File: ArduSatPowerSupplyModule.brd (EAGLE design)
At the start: 95.5 x 90.3 mm, 168 parts, among them IC1 ATmega328P, IC10 TMP102, IC11 TMP102, IC2 ATMEGA16U2-MU, IC3 LTC3115, IC4 LTC4078, IC5 MAX17043G+U, IC6 MAX4372F, IC7 LTC3536, IC8 MAX4372F, IC9 LTC3536, Q1 RJU003N03 N-MOSFET, Q2 RJU003N03 N-MOSFET, Q3 MOSFET-PCHANNELSMT2, Q4 RJU003N03 N-MOSFET, Q5 RJU003N03 N-MOSFET, Q6 RJU003N03 N-MOSFET, Q7 RJU003N03 N-MOSFET, Q8 RJU003N03 N-MOSFET, Q9 RJU003N03 N-MOSFET, SW1 RESET, SW2 SWITCH-SPDT

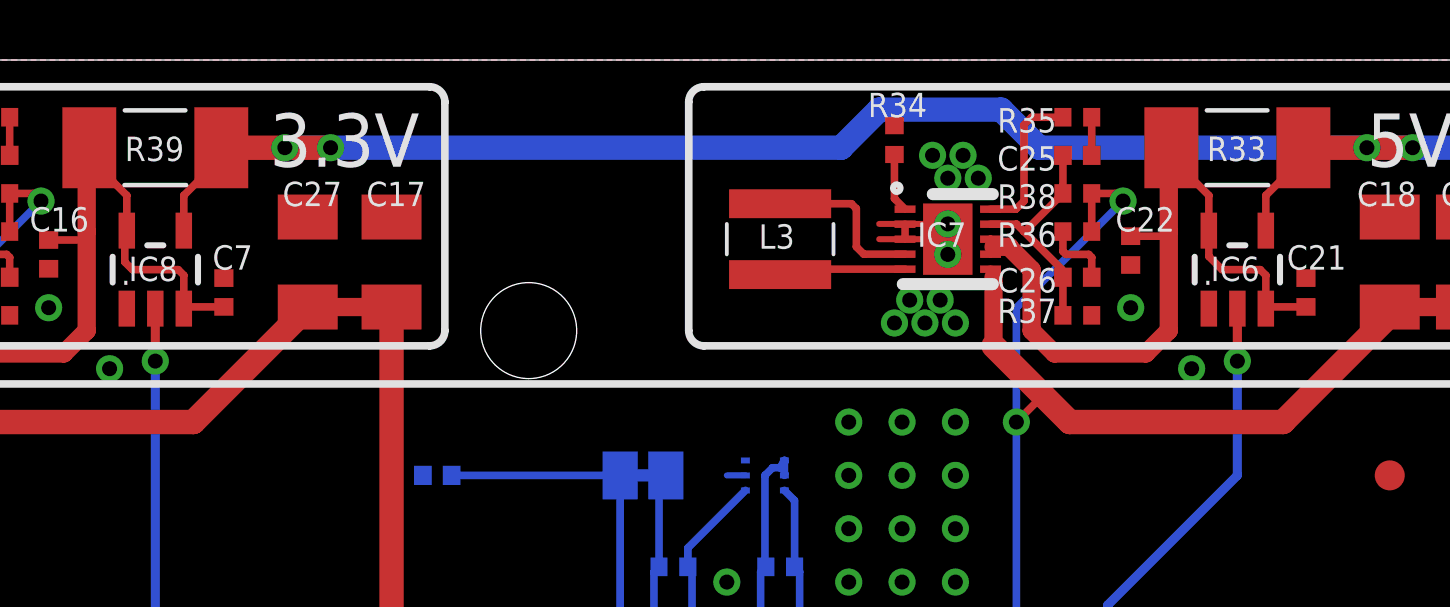
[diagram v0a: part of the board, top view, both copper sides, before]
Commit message: Changed current sense chip VCC to 5V
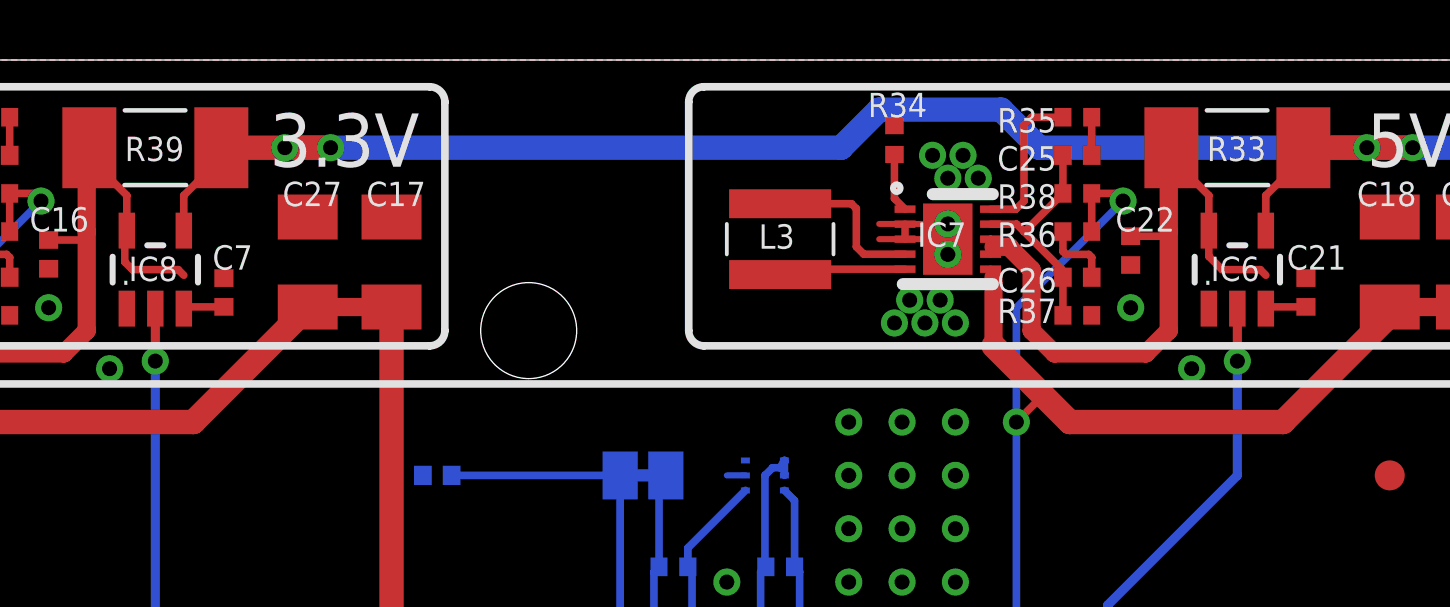
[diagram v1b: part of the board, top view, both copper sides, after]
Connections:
- net 3V3SENSED: no longer C7.1, IC8.3
- net 5V: now also C21.1, C7.1, IC6.3, IC8.3
- net 5VSENSED: no longer C21.1, IC6.3
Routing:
- net 5V: track 232.3 -> 235.0 mm
- net 5VSENSED: track 25.6 -> 23.1 mm
- net 3V3SENSED: track 26.2 -> 23.8 mm
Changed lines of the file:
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@@
 <wire x1="64.008" y1="85.852" x2="63.218" y2="85.852" width="0.254" layer="1"/>
 <contactref element="SJ4" pad="1"/>
-<wire x1="69.596" y1="45.72" x2="69.596" y2="43.18" width="0" layer="19" extent="1-1"/>
+<contactref element="C21" pad="1"/>
+<contactref element="IC6" pad="3"/>
+<wire x1="70.358" y1="82.07" x2="69.0801" y2="82.07" width="0.254" layer="1"/>
+<wire x1="69.0801" y1="82.07" x2="69.022" y2="82.0119" width="0.254" layer="1"/>
+<contactref element="IC8" pad="3"/>
+<contactref element="C7" pad="1"/>
+<wire x1="34.29" y1="82.07" x2="33.0121" y2="82.07" width="0.254" layer="1"/>
+<wire x1="33.0121" y1="82.07" x2="32.954" y2="82.0119" width="0.254" layer="1"/>
+<wire x1="73.152" y1="82.066" x2="70.358" y2="82.07" width="0" layer="19" extent="1-1"/>
+<wire x1="69.596" y1="43.18" x2="69.596" y2="45.72" width="0" layer="19" extent="1-1"/>
+<wire x1="34.29" y1="82.07" x2="48.514" y2="67.056" width="0" layer="19" extent="1-16"/>
 </signal>
 <signal name="N$1">
@@
 </signal>
 <signal name="3V3SENSED">
-<contactref element="IC8" pad="3"/>
-<contactref element="C7" pad="1"/>
 <contactref element="IC8" pad="5"/>
 <contactref element="R39" pad="2"/>
@@
 <contactref element="IC9" pad="8"/>
 <wire x1="23.777" y1="84.328" x2="23.777" y2="83.828" width="0.254" layer="1"/>
-<wire x1="34.29" y1="82.07" x2="33.0121" y2="82.07" width="0.254" layer="1"/>
-<wire x1="33.0121" y1="82.07" x2="32.954" y2="82.0119" width="0.254" layer="1"/>
-<wire x1="32.954" y1="82.0119" x2="32.954" y2="83.124" width="0.254" layer="1"/>
 <wire x1="32.954" y1="83.124" x2="32.766" y2="83.312" width="0.254" layer="1"/>
 <wire x1="32.766" y1="83.312" x2="31.242" y2="83.312" width="0.254" layer="1"/>
@@
 <contactref element="IC7" pad="8"/>
 <contactref element="R33" pad="2"/>
-<contactref element="C21" pad="1"/>
-<contactref element="IC6" pad="3"/>
 <contactref element="IC6" pad="5"/>
 <wire x1="59.845" y1="84.328" x2="59.845" y2="83.828" width="0.254" layer="1"/>
-<wire x1="69.022" y1="82.0119" x2="69.022" y2="83.124" width="0.254" layer="1"/>
 <wire x1="69.022" y1="83.124" x2="68.834" y2="83.312" width="0.254" layer="1"/>
 <wire x1="68.834" y1="83.312" x2="67.564" y2="83.312" width="0.254" layer="1"/>
@@
 <wire x1="66.548" y1="86.36" x2="66.294" y2="86.36" width="0.254" layer="1"/>
 <wire x1="66.294" y1="86.36" x2="65.786" y2="86.868" width="0.254" layer="1"/>
-<wire x1="70.358" y1="82.07" x2="69.0801" y2="82.07" width="0.254" layer="1"/>
-<wire x1="69.0801" y1="82.07" x2="69.022" y2="82.0119" width="0.254" layer="1"/>
 <wire x1="64.516" y1="84.427" x2="65.758" y2="84.427" width="0.254" layer="1"/>
 <wire x1="65.758" y1="84.427" x2="65.786" y2="84.582" width="0.254" layer="1"/>

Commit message: Relabelled board from ArduSat to LibreSat
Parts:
- removed Q3: MOSFET-PCHANNELSMT2, freetronics-jon:DPAK
- removed R27: 1K, freetronics-jon:0402
- removed R28: 33K, freetronics-jon:0402
- R11, R25: value 2K2 0402 -> 3K3 0402
- R12, R26: value 1K 0402 -> 1K5 0402
- moved JP10 10.2 mm to (19.8, 23.4), turned to 90 degrees
- moved JP11 5.08 mm to (19.8, 31.0), turned to 90 degrees
- moved C36 1.27 mm to (40.1, 76.5)
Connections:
- removed net N$4: JP11.2, R27.1
- removed net N$7: Q3.1, R27.2, R28.2
- net A2: no longer SJ19.2
- net A3: no longer SJ18.2
- net A6: now also SJ19.2
- net A7: now also SJ18.2
- net GND: no longer JP10.1
- net N$5: now also JP10.1; no longer Q3.3, R28.1
- net VBATT: now also JP11.2; no longer Q3.2
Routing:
- net A7: track 19.8 -> 47.8 mm
- net A6: track 27.5 -> 52.8 mm
- net A3: track 25.2 -> 6.10 mm
- net A2: track 22.8 -> 5.68 mm
- net N$7: track 7.57 -> 0.00 mm
- net VBATT: track 180.6 -> 187.0 mm
- net N$5: track 11.5 -> 17.7 mm
- net N$4: track 4.85 -> 0.00 mm
- net 3V3SENSED: track 23.8 -> 20.5 mm
- net 5VSENSED: track 23.1 -> 20.1 mm
- net 3.3V: track 345.1 -> 346.4 mm
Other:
- board text added: "A6"
- board text added: "A7"
- board text added: "Copyright 2014 Freetronics www.freetronics.com/lspsm"
- board text added: "Deployment Switch"
- board text added: "Remove-Before-Flight Switch"
- board text added: "Select "Arduino Uno" in the IDE"
- board text added: "tron.cc/lspsm"
- board text added: "www.LibreSat.org"
- board text added: "www.freetronics.com/lspsm"
- board text removed: "/Users/jon/Dropbox/Freetronics/ConsultingProjects/ArduSat/nanosatisfi 2-2 BW.bmp"
- board text removed: "A2"
- board text removed: "A3"
- board text removed: "Copyright 2013 Freetronics www.freetronics.com/aspsm"
- board text removed: "Deployment Interlock"
- board text removed: "RBF Interlock"
- board text removed: "v1.0"
- board text removed: "www.ardusat.org"
- board text removed: "www.freetronics.com/aspsm"
- board text removed: "www.libresat.org"
